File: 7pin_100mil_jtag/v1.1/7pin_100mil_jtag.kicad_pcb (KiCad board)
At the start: 2 copper layers, 20 x 13 mm, 61 parts, among them SW1 TACT, X1 JTAG-10, X2 JTAG-7

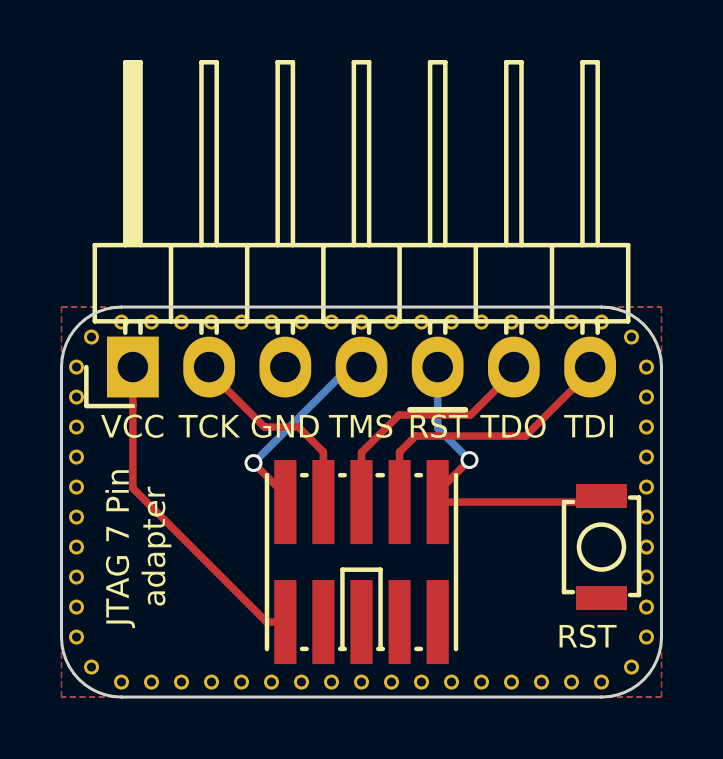
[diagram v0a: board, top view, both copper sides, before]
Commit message: Added a better pin 1 indication to the 10 pin connector.
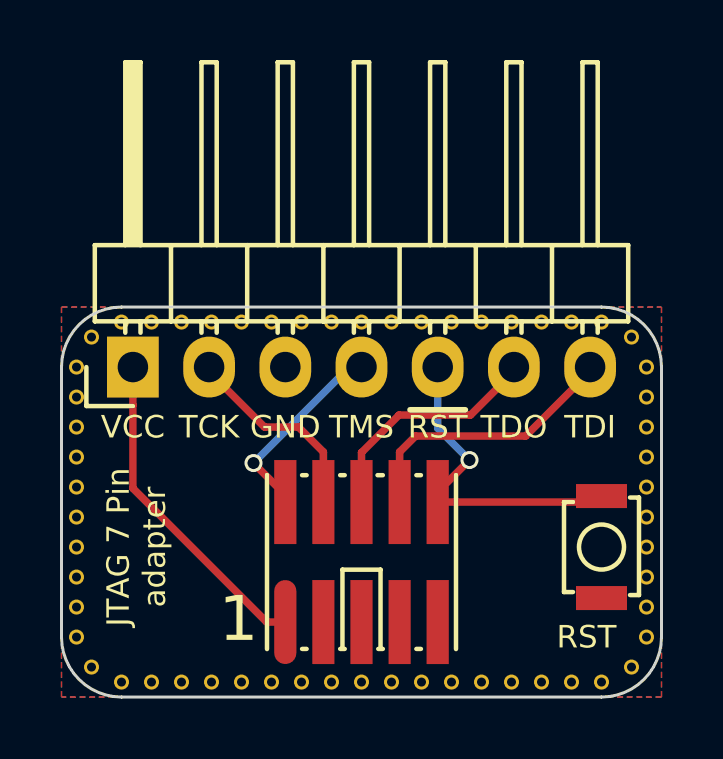
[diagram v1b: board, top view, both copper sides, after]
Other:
- board text added: "1"
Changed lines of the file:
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@@
-(kicad_pcb (version 4) (host pcbnew 4.0.6-e0-6349~53~ubuntu16.04.1)
+(kicad_pcb (version 4) (host pcbnew 4.0.7-e2-6376~58~ubuntu16.04.1)
   (general
     (links 69)
@@
     (area 16.305 23.124999 52.85 51.7)
     (thickness 1.6)
-    (drawings 33)
+    (drawings 34)
     (tracks 31)
     (zones 0)
@@
     (mod_text_size 1 1)
     (mod_text_width 0.15)
-    (pad_size 2.032 1.7272)
-    (pad_drill 1.016)
+    (pad_size 0.74 2.8)
+    (pad_drill 0)
     (pad_to_mask_clearance 0)
     (aux_axis_origin 20 32)
@@
       (drillshape 0)
       (scaleselection 1)
-      (outputdirectory gerber))
+      (outputdirectory 7pin_adapter_gerber))
   )
   (net 0 "")
@@
     (fp_line (start 3.15 2.9) (end 3.15 -2.9) (layer F.SilkS) (width 0.15))
     (fp_line (start -3.15 2.9) (end -3.15 -2.9) (layer F.SilkS) (width 0.15))
-    (pad 1 smd rect (at 2.54 -2) (size 0.74 2.8) (layers F.Cu F.Paste F.Mask)
+    (pad 1 smd oval (at 2.54 -2) (size 0.74 2.8) (layers F.Cu F.Paste F.Mask)
       (net 4 /VCC))
     (pad 2 smd rect (at 2.54 2) (size 0.74 2.8) (layers F.Cu F.Paste F.Mask)
@@
       (net 1 /RST))
   )
+  (gr_text 1 (at 25.9 42.4) (layer F.SilkS)
+    (effects (font (size 1.5 1.5) (thickness 0.3)))
+  )
   (gr_text "(C)2017\n1BitSquared\nCC-BY-SA" (at 38 41.1 90) (layer B.SilkS)
